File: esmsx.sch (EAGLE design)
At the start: 27 parts, among them IC1 XC9536_44VQ, IC2 317EMP, U1 PIC32MX130F064D-I/PT

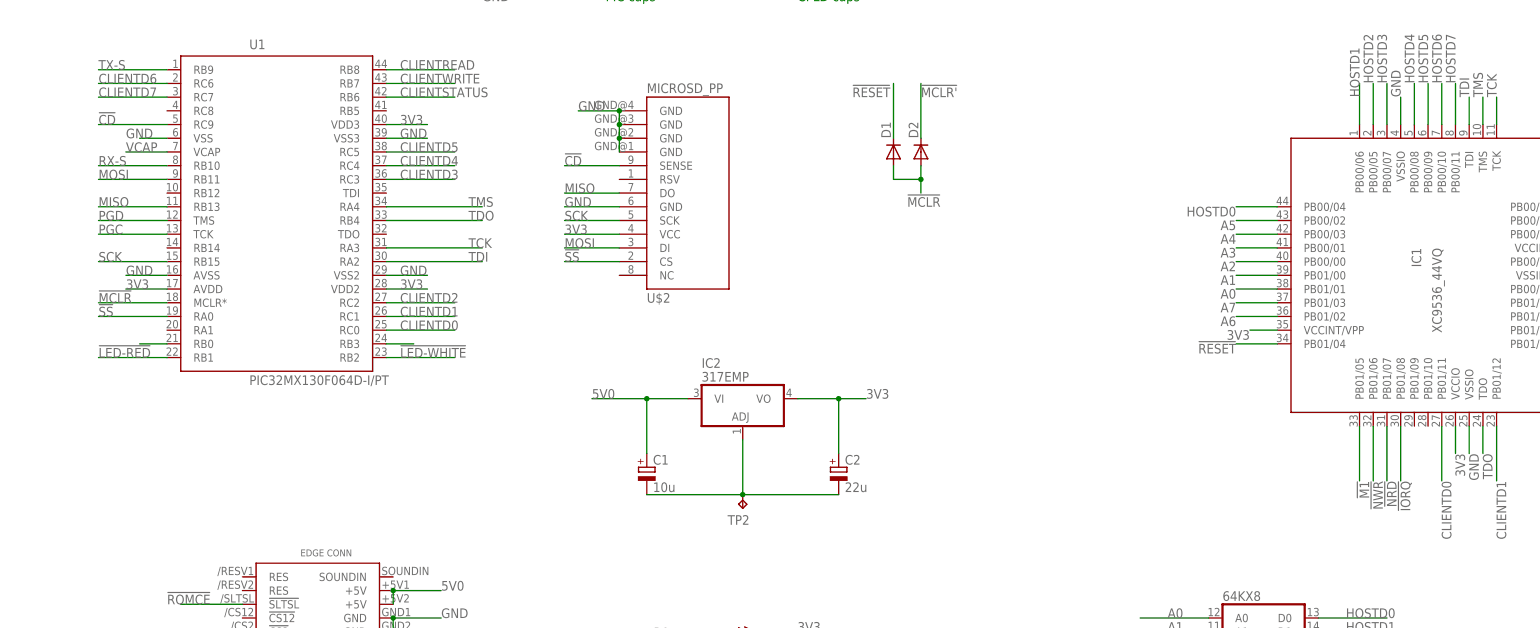
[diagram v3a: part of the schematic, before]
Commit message: broken out pads and current sources for leds
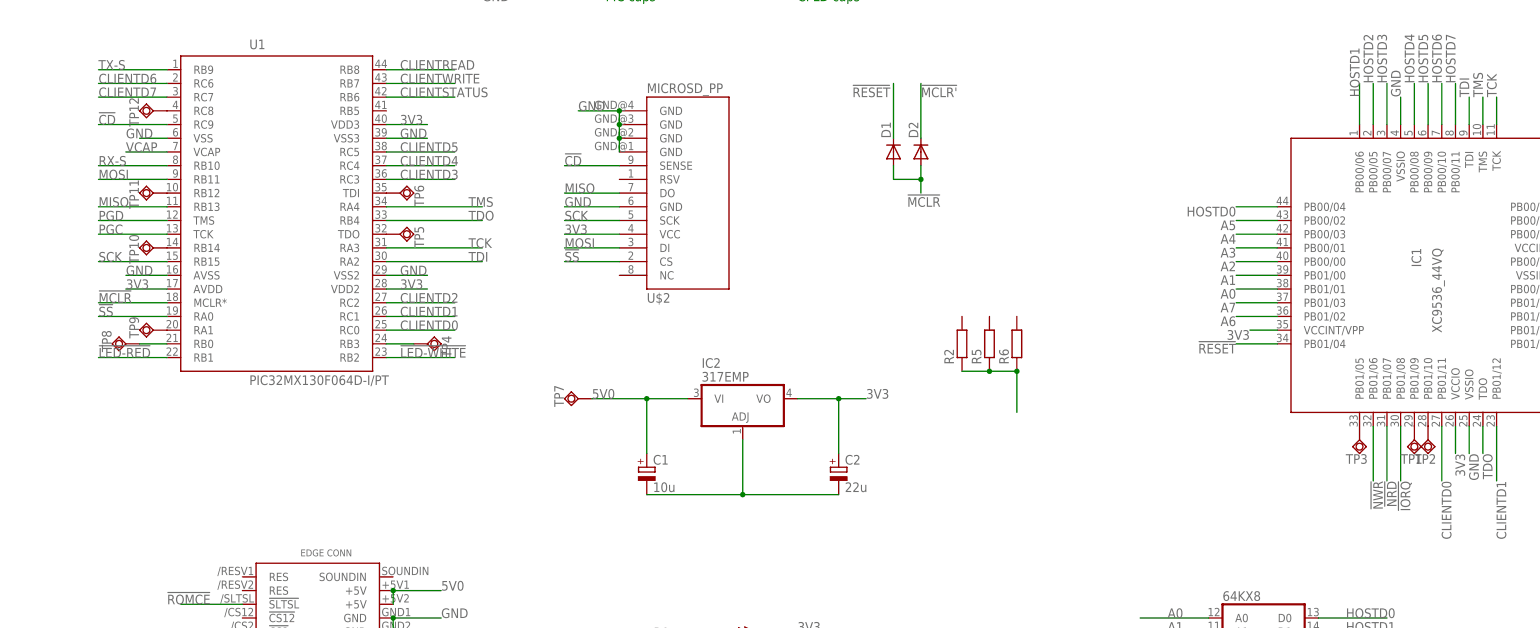
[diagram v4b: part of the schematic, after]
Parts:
- added R2, R5, R6: (no value), resistor:R-EU_R0805W
- added TP1, TP10, TP11, TP12, TP3, TP4, TP5, TP6, TP7, TP8, TP9: TPSQTP20SQ, testpad:TPSQTP20SQ
- TP2: value TPTP17SQ -> TPSQTP20SQ; device testpad:TPTP17SQ -> testpad:TPSQTP20SQ
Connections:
- removed net !M1: IC1.PB01/05
- new net N$10: TP6.TP, U1.TDI
- new net N$12: TP9.TP, U1.RA1
- new net N$13: TP10.TP, U1.RB14
- new net N$14: TP11.TP, U1.RB12
- new net N$15: TP12.TP, U1.RC8
- new net N$6: IC1.PB01/09, TP1.TP
- new net N$7: IC1.PB01/10, TP2.TP
- new net N$8: IC1.PB01/05, TP3.TP
- new net N$9: TP5.TP, U1.TDO
- net 5V0: now also R2.1, R5.1, R6.1, TP7.TP
- net GND: no longer TP2.TP
- net N$4: now also TP8.TP
- net N$5: now also TP4.TP
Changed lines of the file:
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@@
 <part name="U$3" library="SparkFun" deviceset="6PIN" device=""/>
 <part name="U$4" library="smb-microheaders" deviceset="5PIN" device=""/>
-<part name="TP2" library="testpad" deviceset="TP" device="TP17SQ" value="TPTP17SQ"/>
 <part name="JP2" library="pinhead-round" deviceset="PINHD-1X3" device=""/>
 <part name="JP3" library="pinhead-round" deviceset="PINHD-1X3" device=""/>
+<part name="TP1" library="testpad" library_urn="urn:adsk.eagle:library:385" deviceset="TPSQ" device="TP20SQ" package3d_urn="urn:adsk.eagle:package:27980/1"/>
+<part name="TP2" library="testpad" library_urn="urn:adsk.eagle:library:385" deviceset="TPSQ" device="TP20SQ" package3d_urn="urn:adsk.eagle:package:27980/1"/>
+<part name="TP3" library="testpad" library_urn="urn:adsk.eagle:library:385" deviceset="TPSQ" device="TP20SQ" package3d_urn="urn:adsk.eagle:package:27980/1"/>
+<part name="TP4" library="testpad" library_urn="urn:adsk.eagle:library:385" deviceset="TPSQ" device="TP20SQ" package3d_urn="urn:adsk.eagle:package:27980/1"/>
+<part name="TP5" library="testpad" library_urn="urn:adsk.eagle:library:385" deviceset="TPSQ" device="TP20SQ" package3d_urn="urn:adsk.eagle:package:27980/1"/>
+<part name="TP6" library="testpad" library_urn="urn:adsk.eagle:library:385" deviceset="TPSQ" device="TP20SQ" package3d_urn="urn:adsk.eagle:package:27980/1"/>
+<part name="TP8" library="testpad" library_urn="urn:adsk.eagle:library:385" deviceset="TPSQ" device="TP20SQ" package3d_urn="urn:adsk.eagle:package:27980/1"/>
+<part name="TP9" library="testpad" library_urn="urn:adsk.eagle:library:385" deviceset="TPSQ" device="TP20SQ" package3d_urn="urn:adsk.eagle:package:27980/1"/>
+<part name="TP10" library="testpad" library_urn="urn:adsk.eagle:library:385" deviceset="TPSQ" device="TP20SQ" package3d_urn="urn:adsk.eagle:package:27980/1"/>
+<part name="TP11" library="testpad" library_urn="urn:adsk.eagle:library:385" deviceset="TPSQ" device="TP20SQ" package3d_urn="urn:adsk.eagle:package:27980/1"/>
+<part name="TP12" library="testpad" library_urn="urn:adsk.eagle:library:385" deviceset="TPSQ" device="TP20SQ" package3d_urn="urn:adsk.eagle:package:27980/1"/>
+<part name="TP7" library="testpad" library_urn="urn:adsk.eagle:library:385" deviceset="TPSQ" device="TP20SQ" package3d_urn="urn:adsk.eagle:package:27980/1"/>
+<part name="R2" library="resistor" deviceset="R-EU_" device="R0805W"/>
+<part name="R5" library="resistor" deviceset="R-EU_" device="R0805W"/>
+<part name="R6" library="resistor" deviceset="R-EU_" device="R0805W"/>
 </parts>
 <sheets>
@@
 <instance part="U$3" gate="G$1" x="-10.16" y="228.6" rot="R180"/>
 <instance part="U$4" gate="G$1" x="-12.7" y="177.8"/>
-<instance part="TP2" gate="G$1" x="137.16" y="99.06" rot="R180"/>
 <instance part="JP2" gate="A" x="55.88" y="238.76"/>
 <instance part="JP3" gate="A" x="55.88" y="228.6"/>
+<instance part="TP1" gate="G$1" x="261.62" y="111.76"/>
+<instance part="TP2" gate="G$1" x="264.16" y="111.76"/>
+<instance part="TP3" gate="G$1" x="251.46" y="111.76"/>
+<instance part="TP4" gate="G$1" x="78.74" y="129.54" rot="R90"/>
+<instance part="TP5" gate="G$1" x="73.66" y="149.86" rot="R90"/>
+<instance part="TP6" gate="G$1" x="73.66" y="157.48" rot="R90"/>
+<instance part="TP8" gate="G$1" x="22.86" y="129.54" rot="R270"/>
+<instance part="TP9" gate="G$1" x="27.94" y="132.08" rot="R270"/>
+<instance part="TP10" gate="G$1" x="27.94" y="147.32" rot="R270"/>
+<instance part="TP11" gate="G$1" x="27.94" y="157.48" rot="R270"/>
+<instance part="TP12" gate="G$1" x="27.94" y="172.72" rot="R270"/>
+<instance part="TP7" gate="G$1" x="106.68" y="119.38" rot="R270"/>
+<instance part="R2" gate="G$1" x="177.8" y="129.54" rot="R90"/>
+<instance part="R5" gate="G$1" x="182.88" y="129.54" rot="R90"/>
+<instance part="R6" gate="G$1" x="187.96" y="129.54" rot="R90"/>
 </instances>
 <busses>
@@
 <pinref part="C2" gate="G$1" pin="-"/>
 <pinref part="IC2" gate="A1" pin="ADJ"/>
-<pinref part="TP2" gate="G$1" pin="TP"/>
 </segment>
 <segment>
@@
 <label x="109.22" y="119.38" size="1.778" layer="95"/>
 <pinref part="IC2" gate="A1" pin="VI"/>
+<pinref part="TP7" gate="G$1" pin="TP"/>
 </segment>
 <segment>
@@
 <junction x="72.39" y="83.82"/>
 <label x="81.28" y="83.82" size="1.778" layer="95"/>
+</segment>
+<segment>
+<pinref part="R2" gate="G$1" pin="1"/>
+<pinref part="R5" gate="G$1" pin="1"/>
+<wire x1="177.8" y1="124.46" x2="182.88" y2="124.46" width="0.1524" layer="91"/>
+<pinref part="R6" gate="G$1" pin="1"/>
+<wire x1="182.88" y1="124.46" x2="187.96" y2="124.46" width="0.1524" layer="91"/>
+<junction x="182.88" y="124.46"/>
+<wire x1="187.96" y1="124.46" x2="187.96" y2="116.84" width="0.1524" layer="91"/>
+<junction x="187.96" y="124.46"/>
 </segment>
 </net>
@@
 </segment>
 </net>
-<net name="!M1" class="0">
-<segment>
-<pinref part="IC1" gate="G$1" pin="PB01/05"/>
-<wire x1="251.46" y1="114.3" x2="251.46" y2="104.14" width="0.1524" layer="91"/>
-<label x="251.46" y="104.14" size="1.778" layer="95" rot="R270"/>
-</segment>
-</net>
 <net name="MOSI" class="0">
 <segment>
@@
 <pinref part="U1" gate="G$1" pin="RB0"/>
 <wire x1="30.48" y1="129.54" x2="25.4" y2="129.54" width="0.1524" layer="91"/>
+<pinref part="TP8" gate="G$1" pin="TP"/>
 </segment>
 </net>
@@
 <pinref part="U1" gate="G$1" pin="RB3"/>
 <wire x1="71.12" y1="129.54" x2="76.2" y2="129.54" width="0.1524" layer="91"/>
-</segment>
-</net>
+<pinref part="TP4" gate="G$1" pin="TP"/>
+</segment>
+</net>
+<net name="N$6" class="0">
+<segment>
+<pinref part="IC1" gate="G$1" pin="PB01/09"/>
+<pinref part="TP1" gate="G$1" pin="TP"/>
+</segment>
+</net>
+<net name="N$7" class="0">
+<segment>
+<pinref part="IC1" gate="G$1" pin="PB01/10"/>
+<pinref part="TP2" gate="G$1" pin="TP"/>
+</segment>
+</net>
+<net name="N$8" class="0">
+<segment>
+<pinref part="IC1" gate="G$1" pin="PB01/05"/>
+<pinref part="TP3" gate="G$1" pin="TP"/>
+</segment>
+</net>
+<net name="N$9" class="0">
+<segment>
+<pinref part="U1" gate="G$1" pin="TDO"/>
+<pinref part="TP5" gate="G$1" pin="TP"/>
+</segment>
+</net>
+<net name="N$10" class="0">
+<segment>
+<pinref part="U1" gate="G$1" pin="TDI"/>
+<pinref part="TP6" gate="G$1" pin="TP"/>
+</segment>
+</net>
+<net name="N$12" class="0">
+<segment>
+<pinref part="U1" gate="G$1" pin="RA1"/>
+<pinref part="TP9" gate="G$1" pin="TP"/>
+</segment>
+</net>
+<net name="N$13" class="0">
+<segment>
+<pinref part="U1" gate="G$1" pin="RB14"/>
+<pinref part="TP10" gate="G$1" pin="TP"/>
+</segment>
+</net>
+<net name="N$14" class="0">
+<segment>
+<pinref part="U1" gate="G$1" pin="RB12"/>
+<pinref part="TP11" gate="G$1" pin="TP"/>
+</segment>
+</net>
+<net name="N$15" class="0">
+<segment>
+<pinref part="U1" gate="G$1" pin="RC8"/>
+<pinref part="TP12" gate="G$1" pin="TP"/>
+</segment>
+</net>

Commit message: ordered 29 06 protoype 1
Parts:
- removed TP4: TPSQTP20SQ, testpad:TPSQTP20SQ
- added JMP1: 0R-JUMPA, jump-0r-smd:0R-JUMPA
- added LED3: (no value), led:LEDCHIPLED_1206
- added R7: (no value), resistor:R-EU_R0805W
- renumbered LED-RED to LED1, LED-WHITE to LED2
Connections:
- removed net N$3: 64KX8G$1.!WE
- removed net N$5: TP4.TP, U1.RB3
- new net LED-BLUE: R7.1, U1.RB3
- new net N$11: LED3.C, R7.2
- net !NWR: now also JMP1-0R.3
- net 3V3: now also LED3.A
- net 5V0: now also 64KX8G$1.!WE, 64KX8P.VCC, JMP1-0R.1, JMP1-0R.2
- net GND: now also 64KX8P.GND
- net RX-S: now also JP3.1; no longer JP3.2
- net TX-S: now also JP3.2; no longer JP3.1

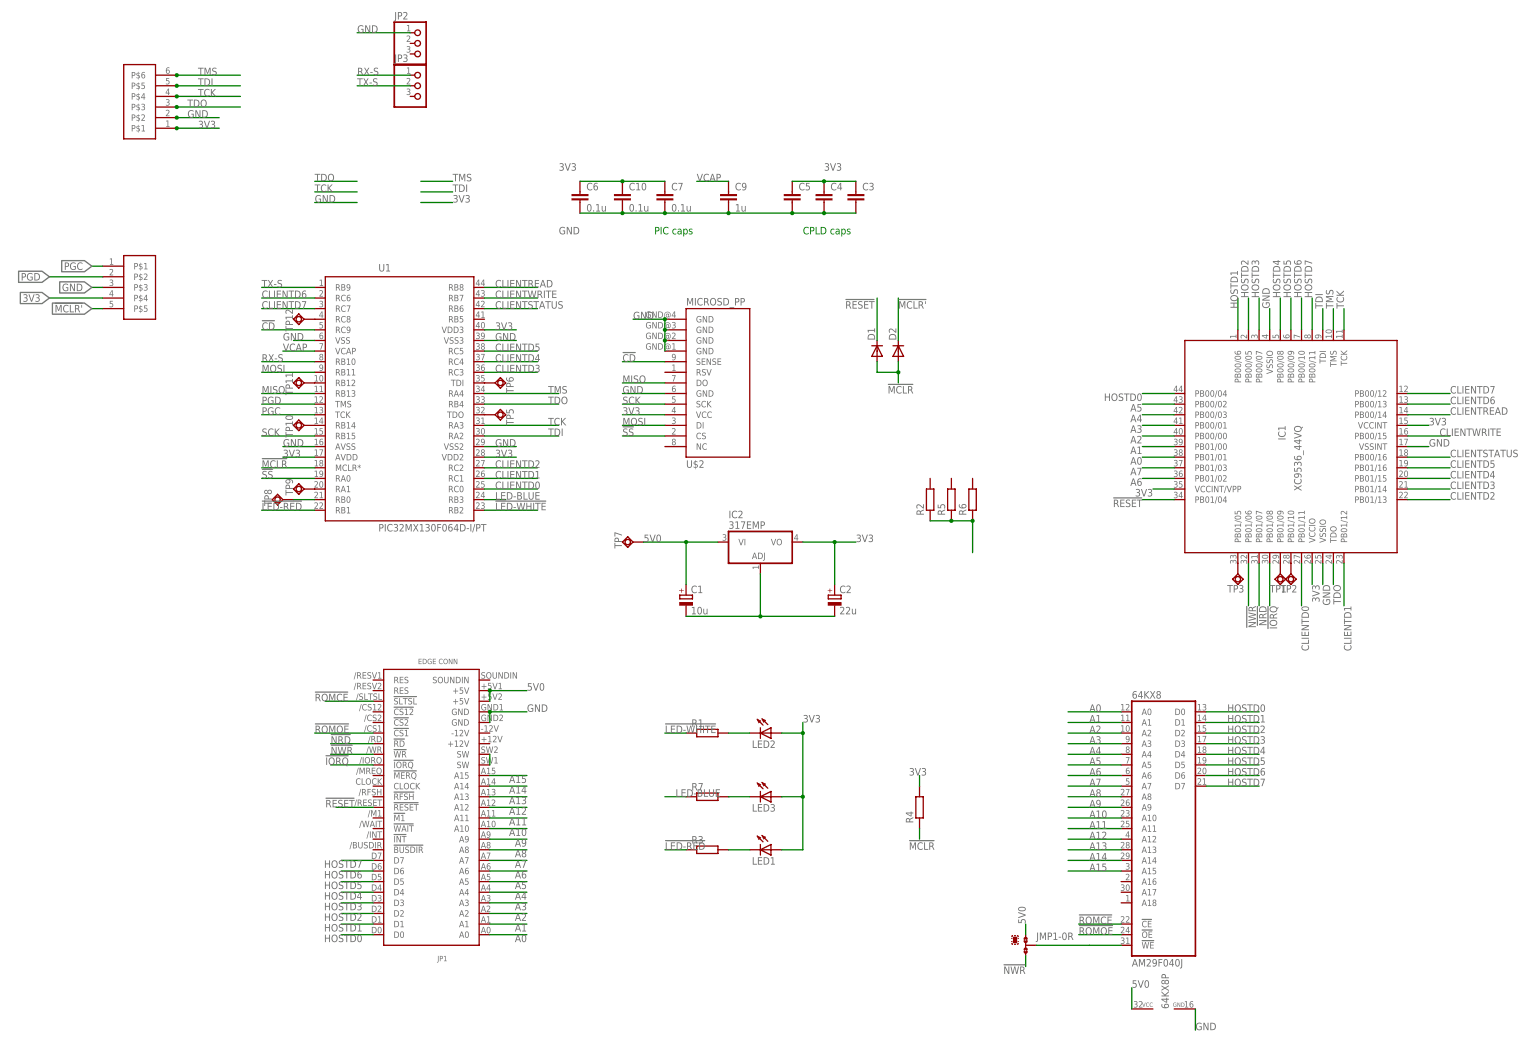
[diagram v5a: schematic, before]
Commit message: name parts in schematic
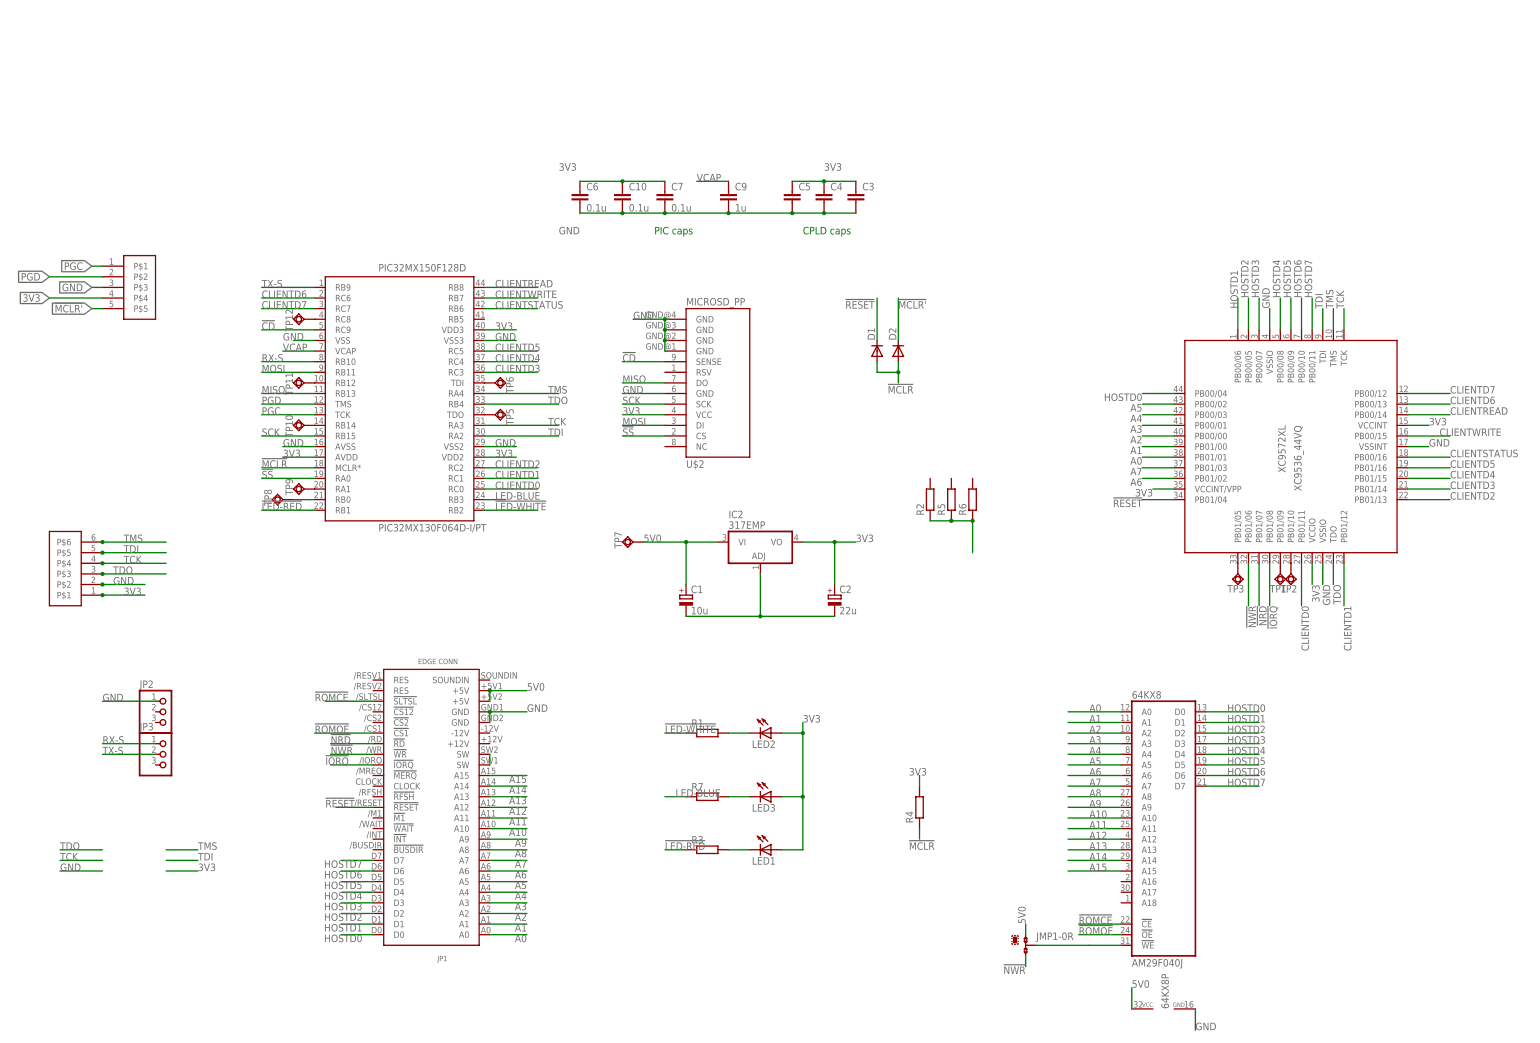
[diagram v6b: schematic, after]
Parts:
- renumbered IC1 to XC9572XL, U1 to PIC32MX150F128D
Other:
- moved on the sheet: JP2, JP3

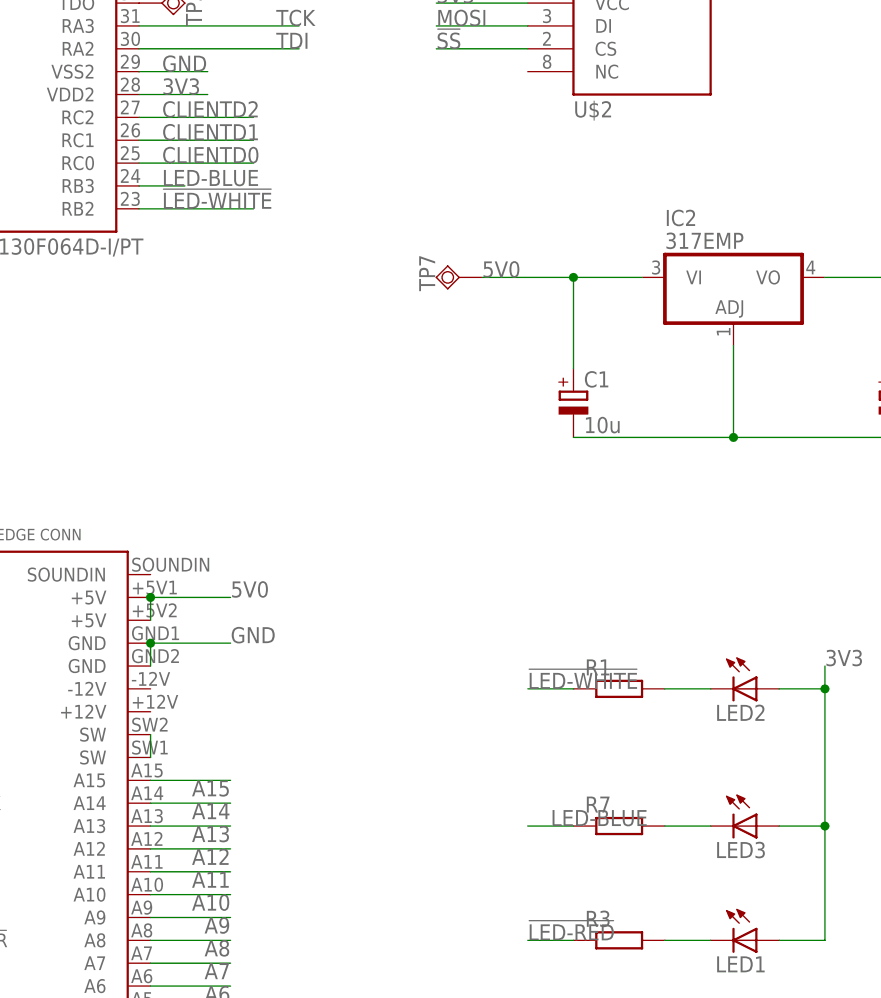
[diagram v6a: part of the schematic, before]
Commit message: led section and renaming signal
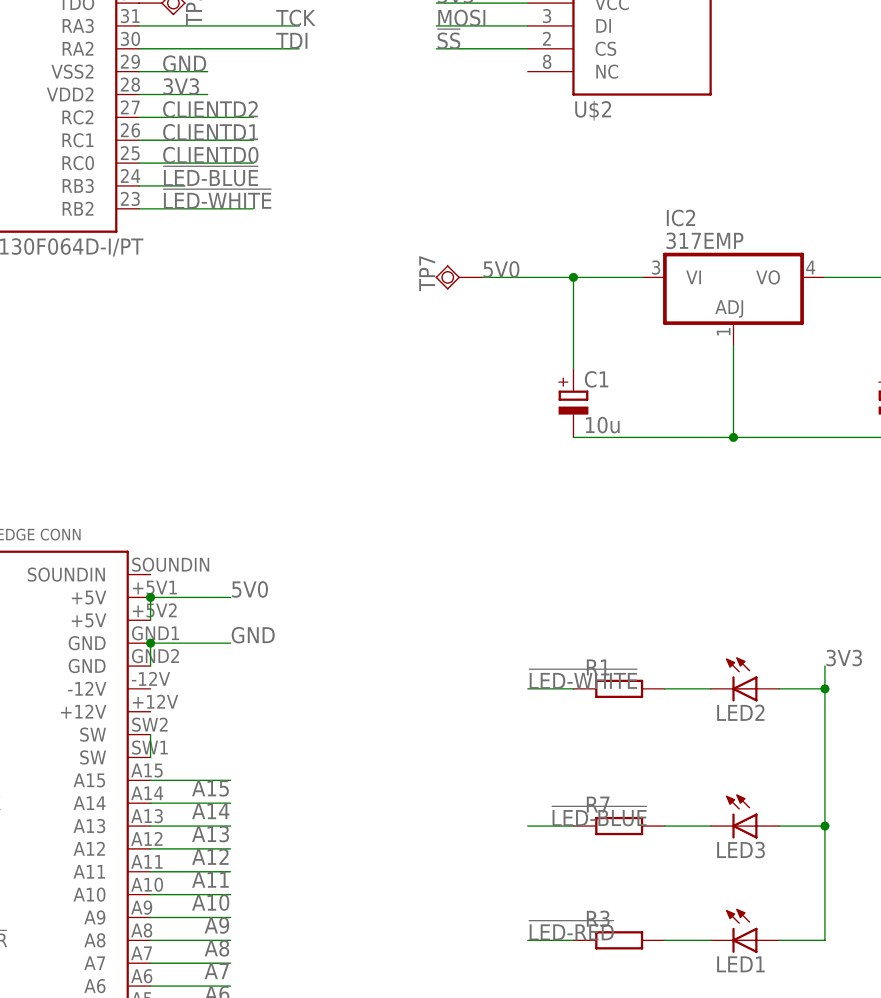
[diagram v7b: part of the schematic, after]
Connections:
- net LED-BLUE renamed !LED-BLUE
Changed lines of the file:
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@@
 </segment>
 </net>
-<net name="LED-BLUE" class="0">
+<net name="!LED-BLUE" class="0">
 <segment>
 <pinref part="PIC32MX150F128D" gate="G$1" pin="RB3"/>
